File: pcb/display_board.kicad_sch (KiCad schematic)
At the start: 49 parts

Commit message: Further schematic capture
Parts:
- removed D? (x4): GREEN, symbol Device:LED
- added D? (x7): GREEN, symbol Device:LED
- added H? (x2): M3, MountingHole:MountingHole_3.2mm_M3_Pad, symbol Mechanical:MountingHole_Pad
- added R?: 330, symbol Device:R
- added SW?: SAMPLE RATE, symbol Switch:SW_Push
- added SW?: LOOPBACK, symbol Switch:SW_Push
- D?: value GREEN -> RED
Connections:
- net COM1: now also D?.1 (K)
- net COM2: now also D?.1 (K)
- net COM3: now also D?.1 (K)
- net COM4: now also D?.1 (K)
- net COM5: now also D?.1 (K)
- net COM6: now also D?.1 (K)
- net COM7: now also D?.1 (K)
- net DISPLAY_GND: now also SW?.2, SW?.2
- net LED20: now also R?.2; no longer R?.2
- net at R?.1: now also U?.56 (ROW21); no longer U?.57 (ROW20)
- net SW_SR: now reaches J?.7 (SW_SR)
- net SW_SR: now also SW?.1
- net SW_LB: now reaches J?.8 (SW_LB)
- net SW_LB: now also SW?.1
- new net: R?.1, U?.57 (ROW20)
- new net GND: H?.1, H?.1
- new net LED21: D?.2 (A), D?.2 (A), D?.2 (A), D?.2 (A), D?.2 (A), D?.2 (A), D?.2 (A), R?.2
- no-connect marks 25 -> 24
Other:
- moved on the sheet: D?, R?

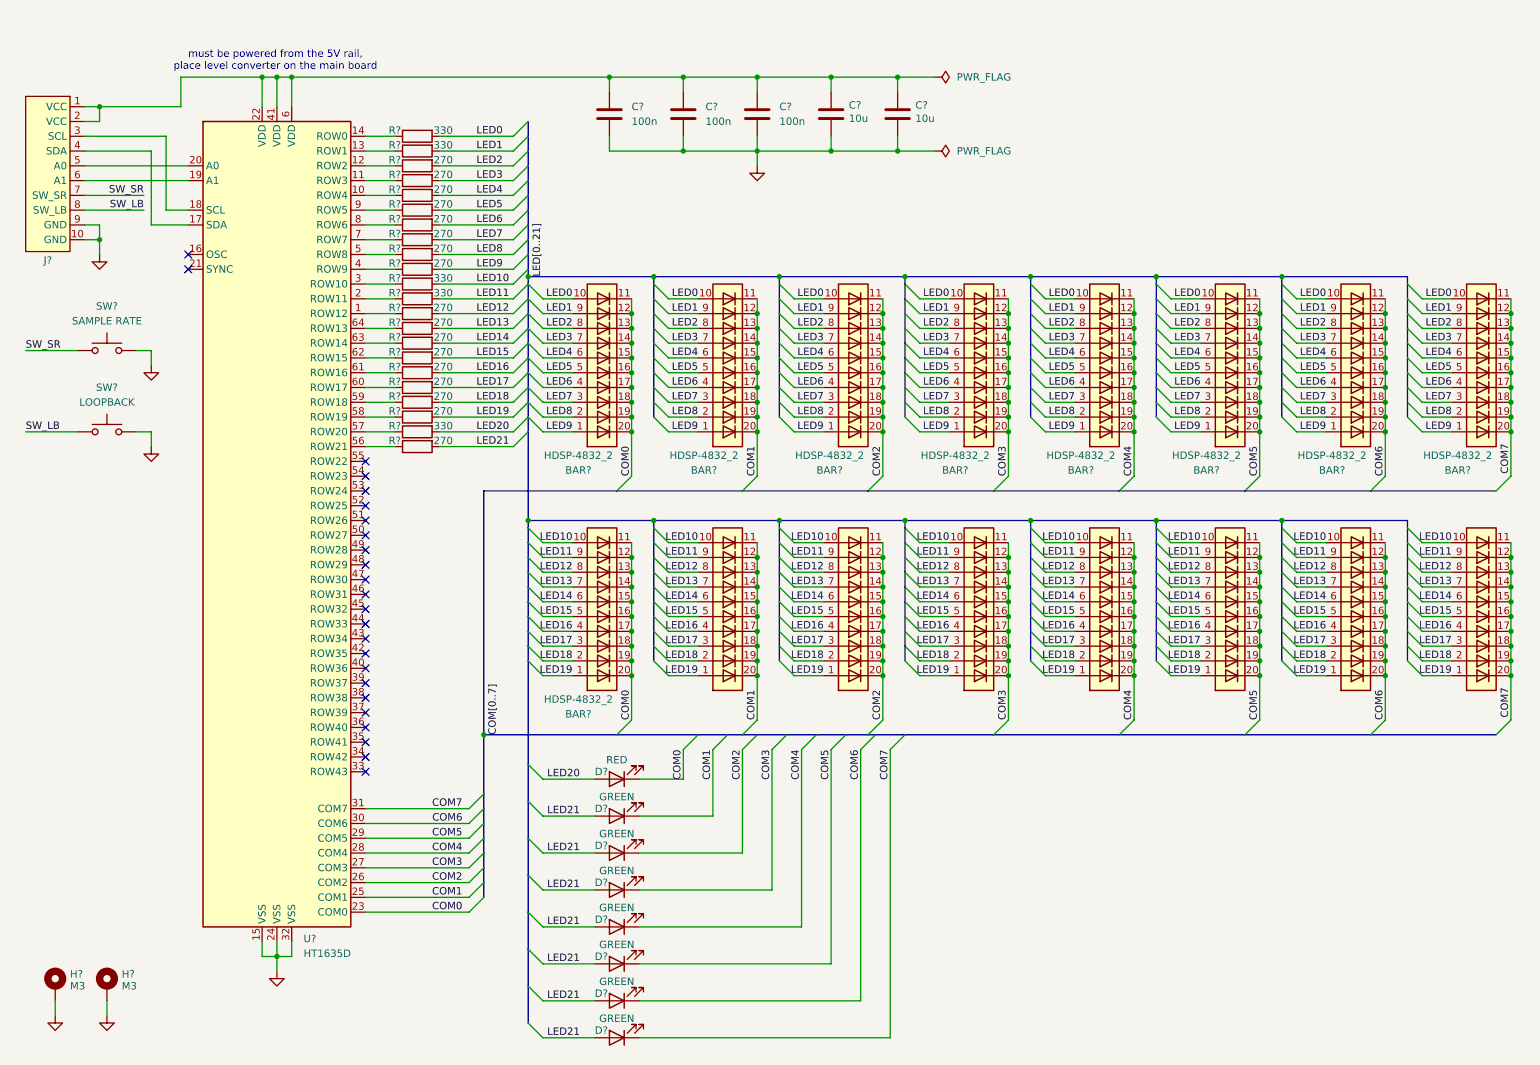
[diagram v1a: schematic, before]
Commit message: Assign most of the footprints to schematic components
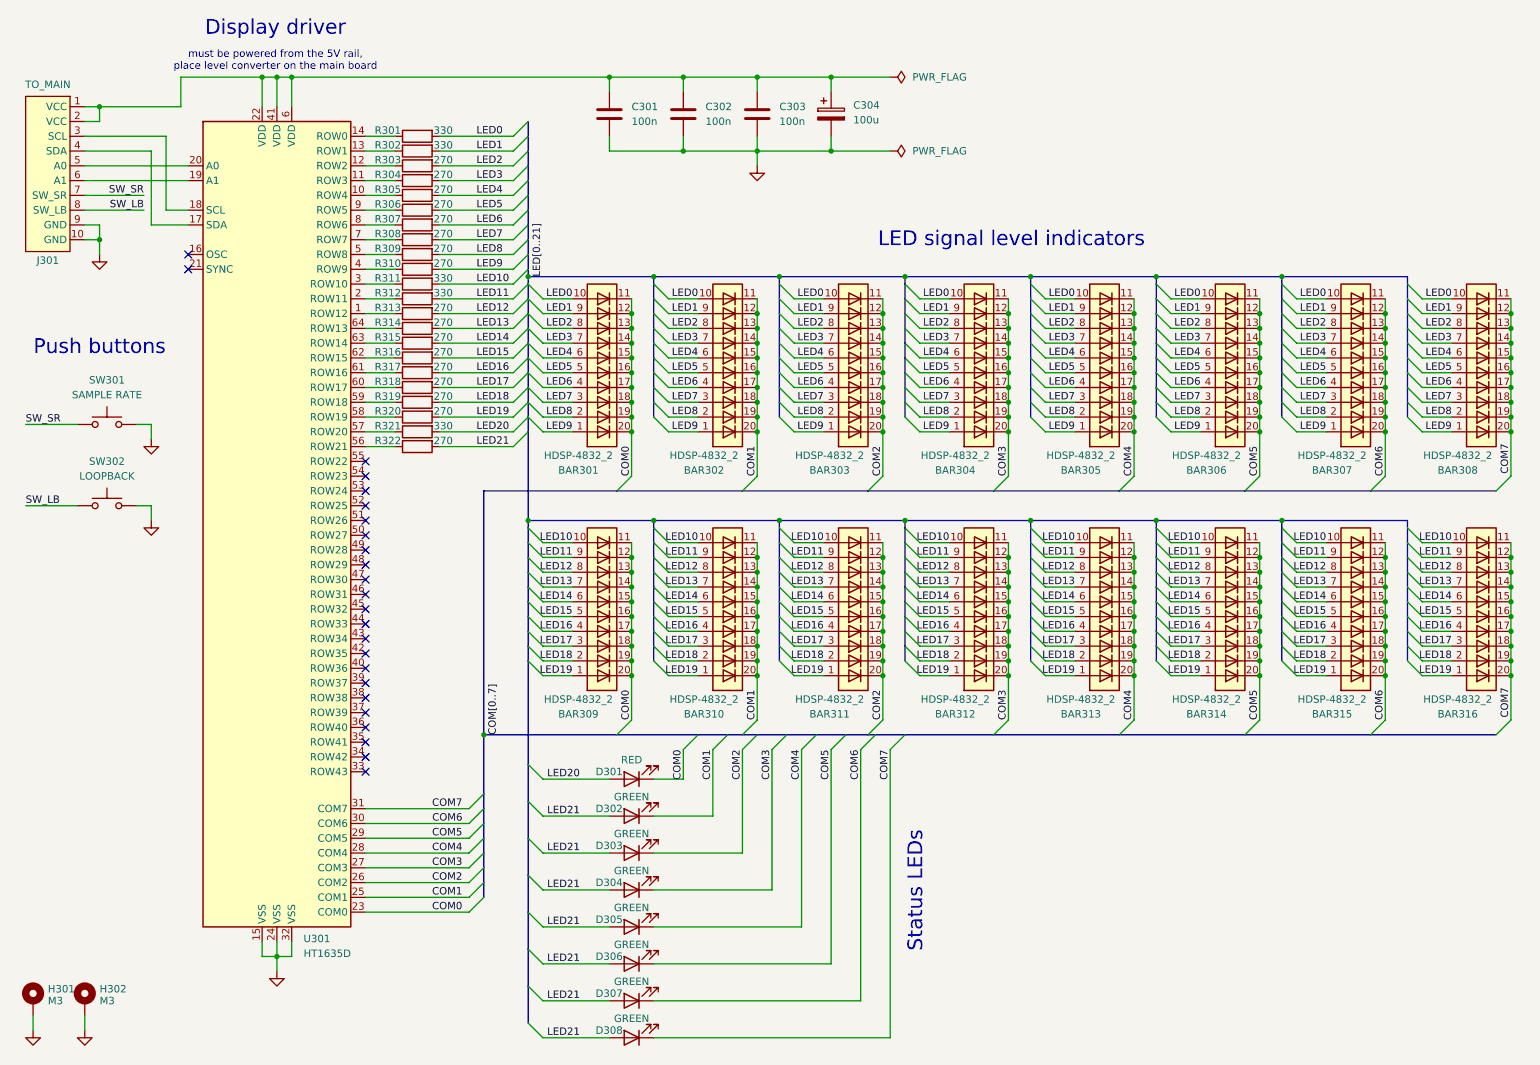
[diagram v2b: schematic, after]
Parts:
- removed BAR? (x7): HDSP-4832_2, Display:HDSP-4832, symbol LED:HDSP-4832_2
- removed C? (x2): 10u, symbol Device:C
- added BAR310, BAR311, BAR312, BAR313, BAR314, BAR315, BAR316: HDSP-4832_2, Display:HDSP-4832, symbol LED:HDSP-4832_2
- added C304: 100u, Capacitor_SMD:C_Elec_6.3x5.4, symbol Device:C_Polarized
- C301, C302, C303: renamed from C?; footprint (none) -> Capacitor_SMD:C_0805_2012Metric_Pad1.18x1.45mm_HandSolder
- D301, D302, D303, D304, D305, D306, D307, D308: renamed from D?; footprint (none) -> adatv2:LED_THT_W7.0mm_H2.00mm
- J301: renamed from J?; value ~ -> TO_MAIN; footprint (none) -> Connector_IDC:IDC-Header_2x05_P2.54mm_Vertical
- R301, R302, R303, R304, R305, R306, R307, R308, R309, R310, R311, R312, R313, R314, R315, R316, R317, R318, R319, R320, R321, R322: renamed from R?; footprint (none) -> Resistor_SMD:R_0805_2012Metric_Pad1.20x1.40mm_HandSolder
- gave numbers to parts that had none: 14
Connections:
- net COM1: now also BAR310.11 (K), BAR310.12 (K), BAR310.13 (K), BAR310.14 (K), BAR310.15 (K), BAR310.16 (K), BAR310.17 (K), BAR310.18 (K), BAR310.19 (K), BAR310.20 (K)
- net COM2: now also BAR311.11 (K), BAR311.12 (K), BAR311.13 (K), BAR311.14 (K), BAR311.15 (K), BAR311.16 (K), BAR311.17 (K), BAR311.18 (K), BAR311.19 (K), BAR311.20 (K)
- net COM3: now also BAR312.11 (K), BAR312.12 (K), BAR312.13 (K), BAR312.14 (K), BAR312.15 (K), BAR312.16 (K), BAR312.17 (K), BAR312.18 (K), BAR312.19 (K), BAR312.20 (K)
- net COM4: now also BAR313.11 (K), BAR313.12 (K), BAR313.13 (K), BAR313.14 (K), BAR313.15 (K), BAR313.16 (K), BAR313.17 (K), BAR313.18 (K), BAR313.19 (K), BAR313.20 (K)
- net COM5: now also BAR314.11 (K), BAR314.12 (K), BAR314.13 (K), BAR314.14 (K), BAR314.15 (K), BAR314.16 (K), BAR314.17 (K), BAR314.18 (K), BAR314.19 (K), BAR314.20 (K)
- net COM6: now also BAR315.11 (K), BAR315.12 (K), BAR315.13 (K), BAR315.14 (K), BAR315.15 (K), BAR315.16 (K), BAR315.17 (K), BAR315.18 (K), BAR315.19 (K), BAR315.20 (K)
- net COM7: now also BAR316.11 (K), BAR316.12 (K), BAR316.13 (K), BAR316.14 (K), BAR316.15 (K), BAR316.16 (K), BAR316.17 (K), BAR316.18 (K), BAR316.19 (K), BAR316.20 (K)
- net DISPLAY_GND: now also C304.2
- net LED10: now also BAR310.10 (A), BAR311.10 (A), BAR312.10 (A), BAR313.10 (A), BAR314.10 (A), BAR315.10 (A), BAR316.10 (A)
- net LED11: now also BAR310.9 (A), BAR311.9 (A), BAR312.9 (A), BAR313.9 (A), BAR314.9 (A), BAR315.9 (A), BAR316.9 (A)
- net LED12: now also BAR310.8 (A), BAR311.8 (A), BAR312.8 (A), BAR313.8 (A), BAR314.8 (A), BAR315.8 (A), BAR316.8 (A)
- net LED13: now also BAR310.7 (A), BAR311.7 (A), BAR312.7 (A), BAR313.7 (A), BAR314.7 (A), BAR315.7 (A), BAR316.7 (A)
- net LED14: now also BAR310.6 (A), BAR311.6 (A), BAR312.6 (A), BAR313.6 (A), BAR314.6 (A), BAR315.6 (A), BAR316.6 (A)
- net LED15: now also BAR310.5 (A), BAR311.5 (A), BAR312.5 (A), BAR313.5 (A), BAR314.5 (A), BAR315.5 (A), BAR316.5 (A)
- net LED16: now also BAR310.4 (A), BAR311.4 (A), BAR312.4 (A), BAR313.4 (A), BAR314.4 (A), BAR315.4 (A), BAR316.4 (A)
- net LED17: now also BAR310.3 (A), BAR311.3 (A), BAR312.3 (A), BAR313.3 (A), BAR314.3 (A), BAR315.3 (A), BAR316.3 (A)
- net LED18: now also BAR310.2 (A), BAR311.2 (A), BAR312.2 (A), BAR313.2 (A), BAR314.2 (A), BAR315.2 (A), BAR316.2 (A)
- net LED19: now also BAR310.1 (A), BAR311.1 (A), BAR312.1 (A), BAR313.1 (A), BAR314.1 (A), BAR315.1 (A), BAR316.1 (A)
- net at C301.1, C302.1, C303.1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: now also C304.1
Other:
- note added: "Display driver"
- note added: "LED signal level indicators"
- note added: "Push buttons"
- note added: "Status LEDs"
- moved on the sheet: D301, D302, D303, D304, D305, D306, D307, D308, H301, H302, SW301, SW302

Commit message: Finish assigning footprints to project
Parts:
- SW301, SW302: footprint (none) -> Button_Switch_SMD:SW_Push_1P1T_NO_CK_PTS125Sx43SMTR
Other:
- note added: "C3040705"
- note added: "C5148424"
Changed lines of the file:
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@@
 		(comment 1 "Drawn by Łukasz Świszcz")
 	)
+	(text "C3040705"
+		(exclude_from_sim no)
+		(at 70.866 178.816 0)
+		(effects
+			(font
+				(size 1.27 1.27)
+			)
+		)
+	)
 	(text "Status LEDs"
 		(exclude_from_sim no)
@@
 		)
 	)
+	(text "C5148424"
+		(exclude_from_sim no)
+		(at 27.94 102.87 0)
+		(effects
+			(font
+				(size 1.27 1.27)
+			)
+			(justify left)
+		)
+	)
 	(text "must be powered from the 5V rail,\nplace level converter on the main board"
 		(exclude_from_sim no)
@@
 			)
 		)
-		(property "Footprint" ""
+		(property "Footprint" "Button_Switch_SMD:SW_Push_1P1T_NO_CK_PTS125Sx43SMTR"
 			(at 33.02 80.01 0)
 			(effects
@@
 			)
 		)
-		(property "Footprint" ""
+		(property "Footprint" "Button_Switch_SMD:SW_Push_1P1T_NO_CK_PTS125Sx43SMTR"
 			(at 33.02 93.98 0)
 			(effects

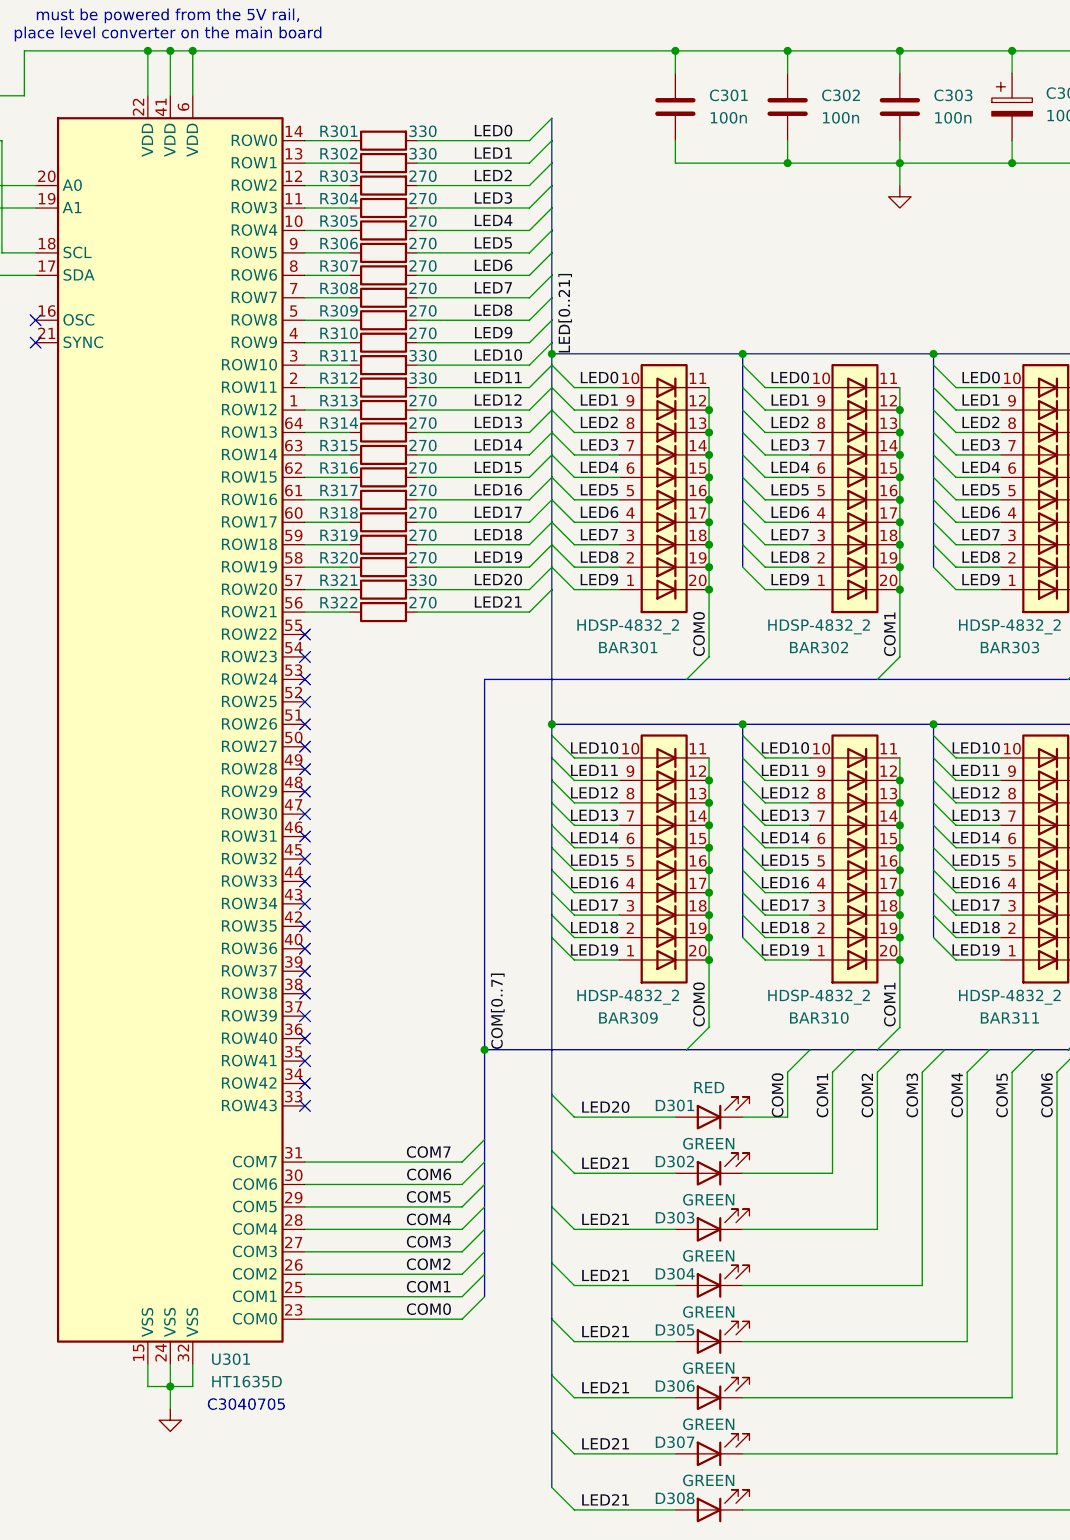
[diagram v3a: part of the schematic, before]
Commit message: Finish drawing IO/Supply board
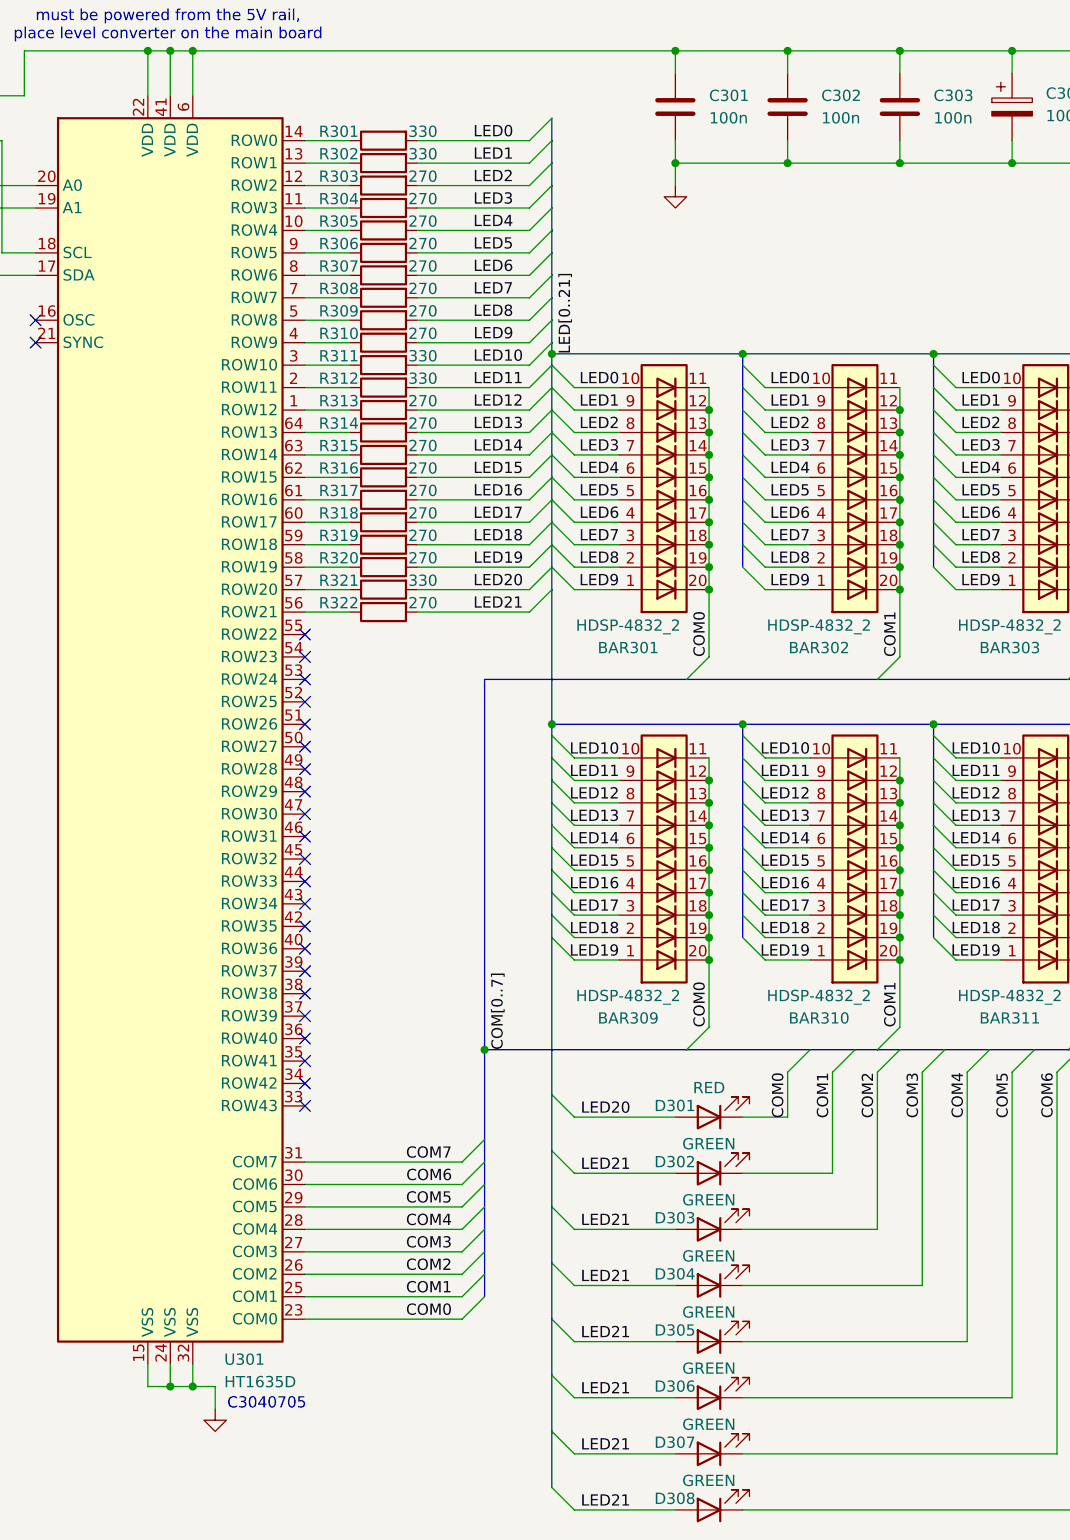
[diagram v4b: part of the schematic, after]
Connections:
- net GND is gone; now on net DISPLAY_GND: H301.1, H302.1
